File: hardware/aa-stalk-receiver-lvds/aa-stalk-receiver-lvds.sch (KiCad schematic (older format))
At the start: 65 parts, among them CN1 Conn_01x02, CN10 Conn_01x03, CN2 Conn_01x04, CN3 6P6C, CN4 Conn_01x03, CN5 Conn_01x02, CN6 Conn_01x02, CN7 Conn_01x02, CN8 Conn_01x02, CN9 Conn_01x03, Q1 KST10, Q2 MCH3484, Q3 MCH3484, U1 AZ1117-5.0, U2 MIC5504-3.3YM5, U3 LM4562, U4 FIN1028, U5 MC3486N

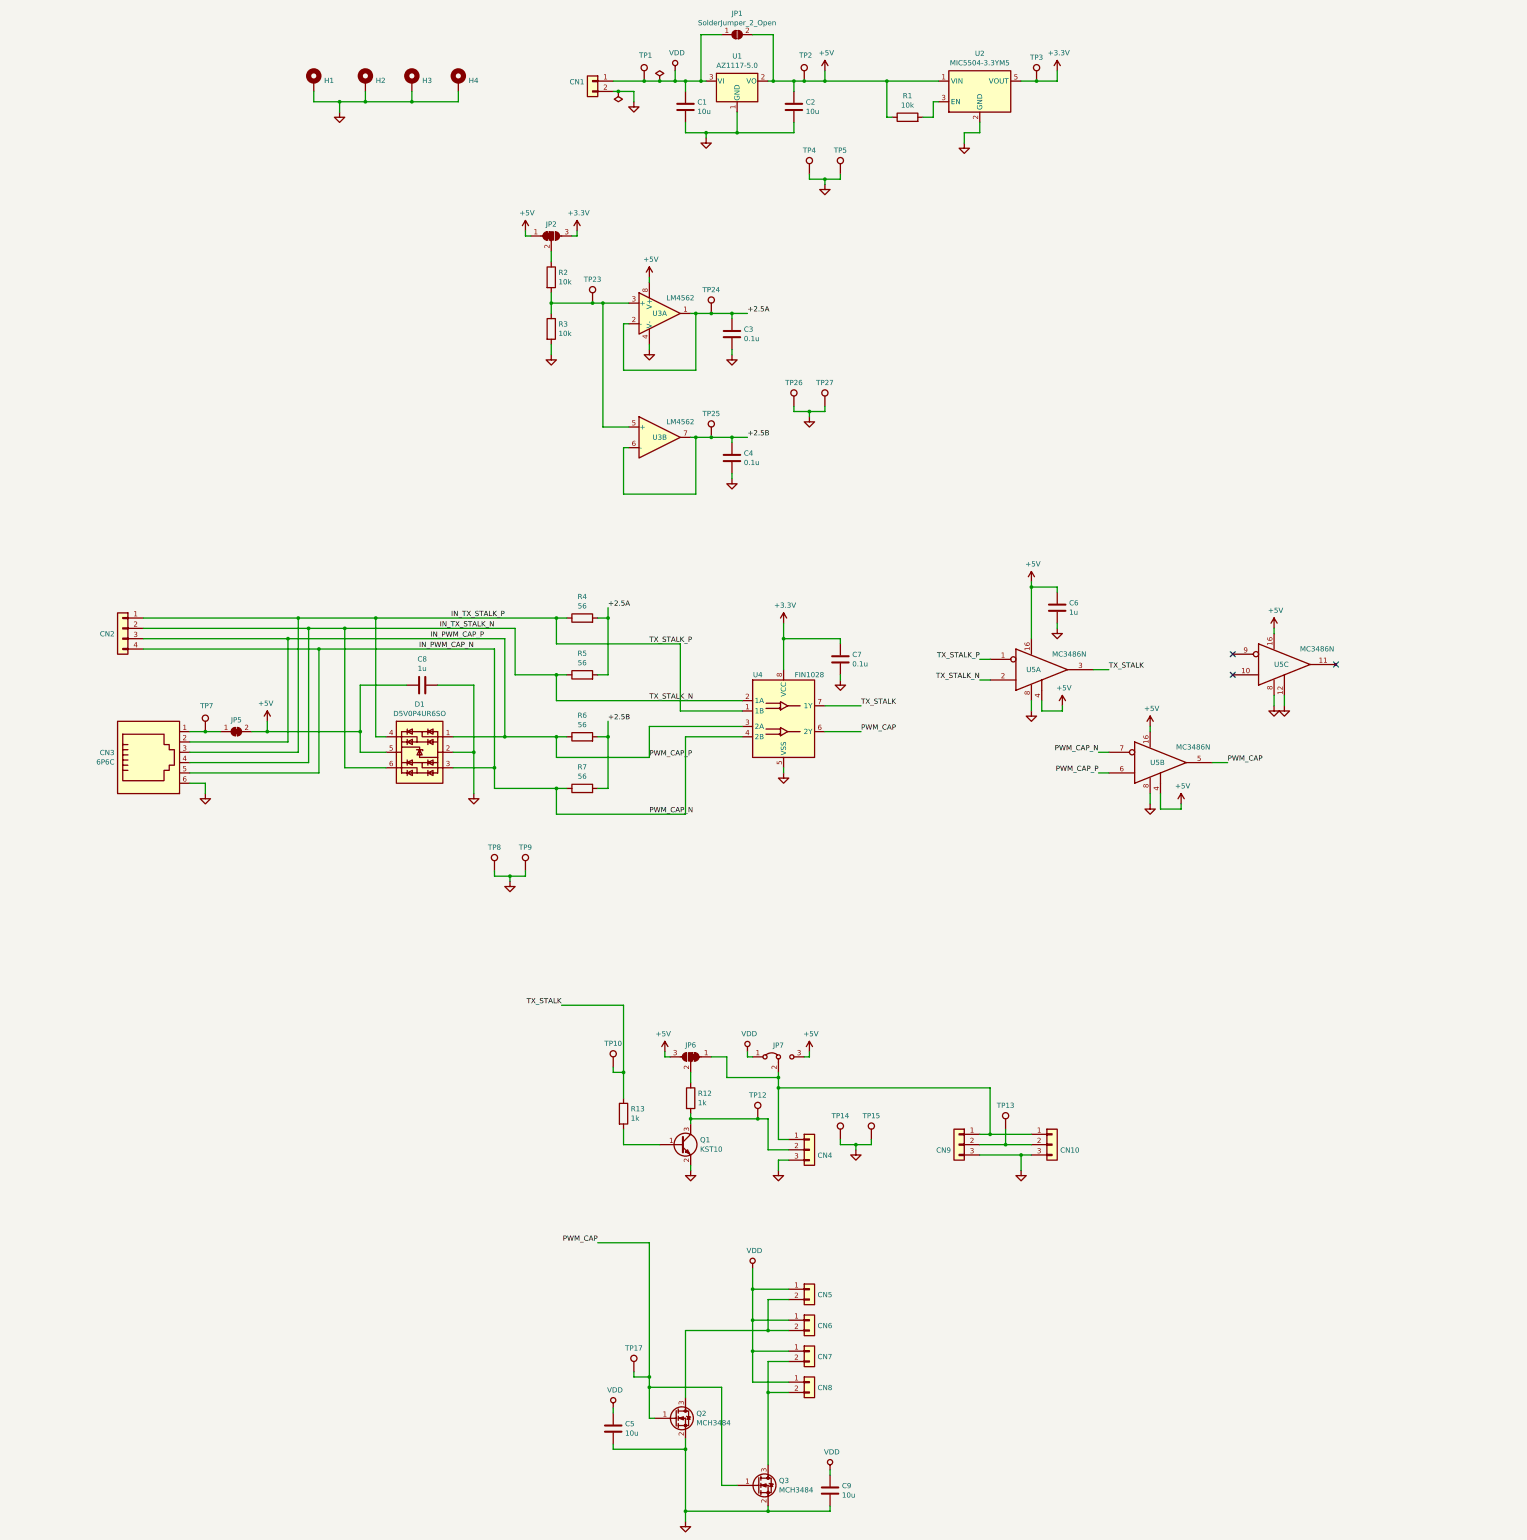
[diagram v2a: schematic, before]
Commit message: Add power distro board, resolve some todos, finish a coherent layout of the panel receiver
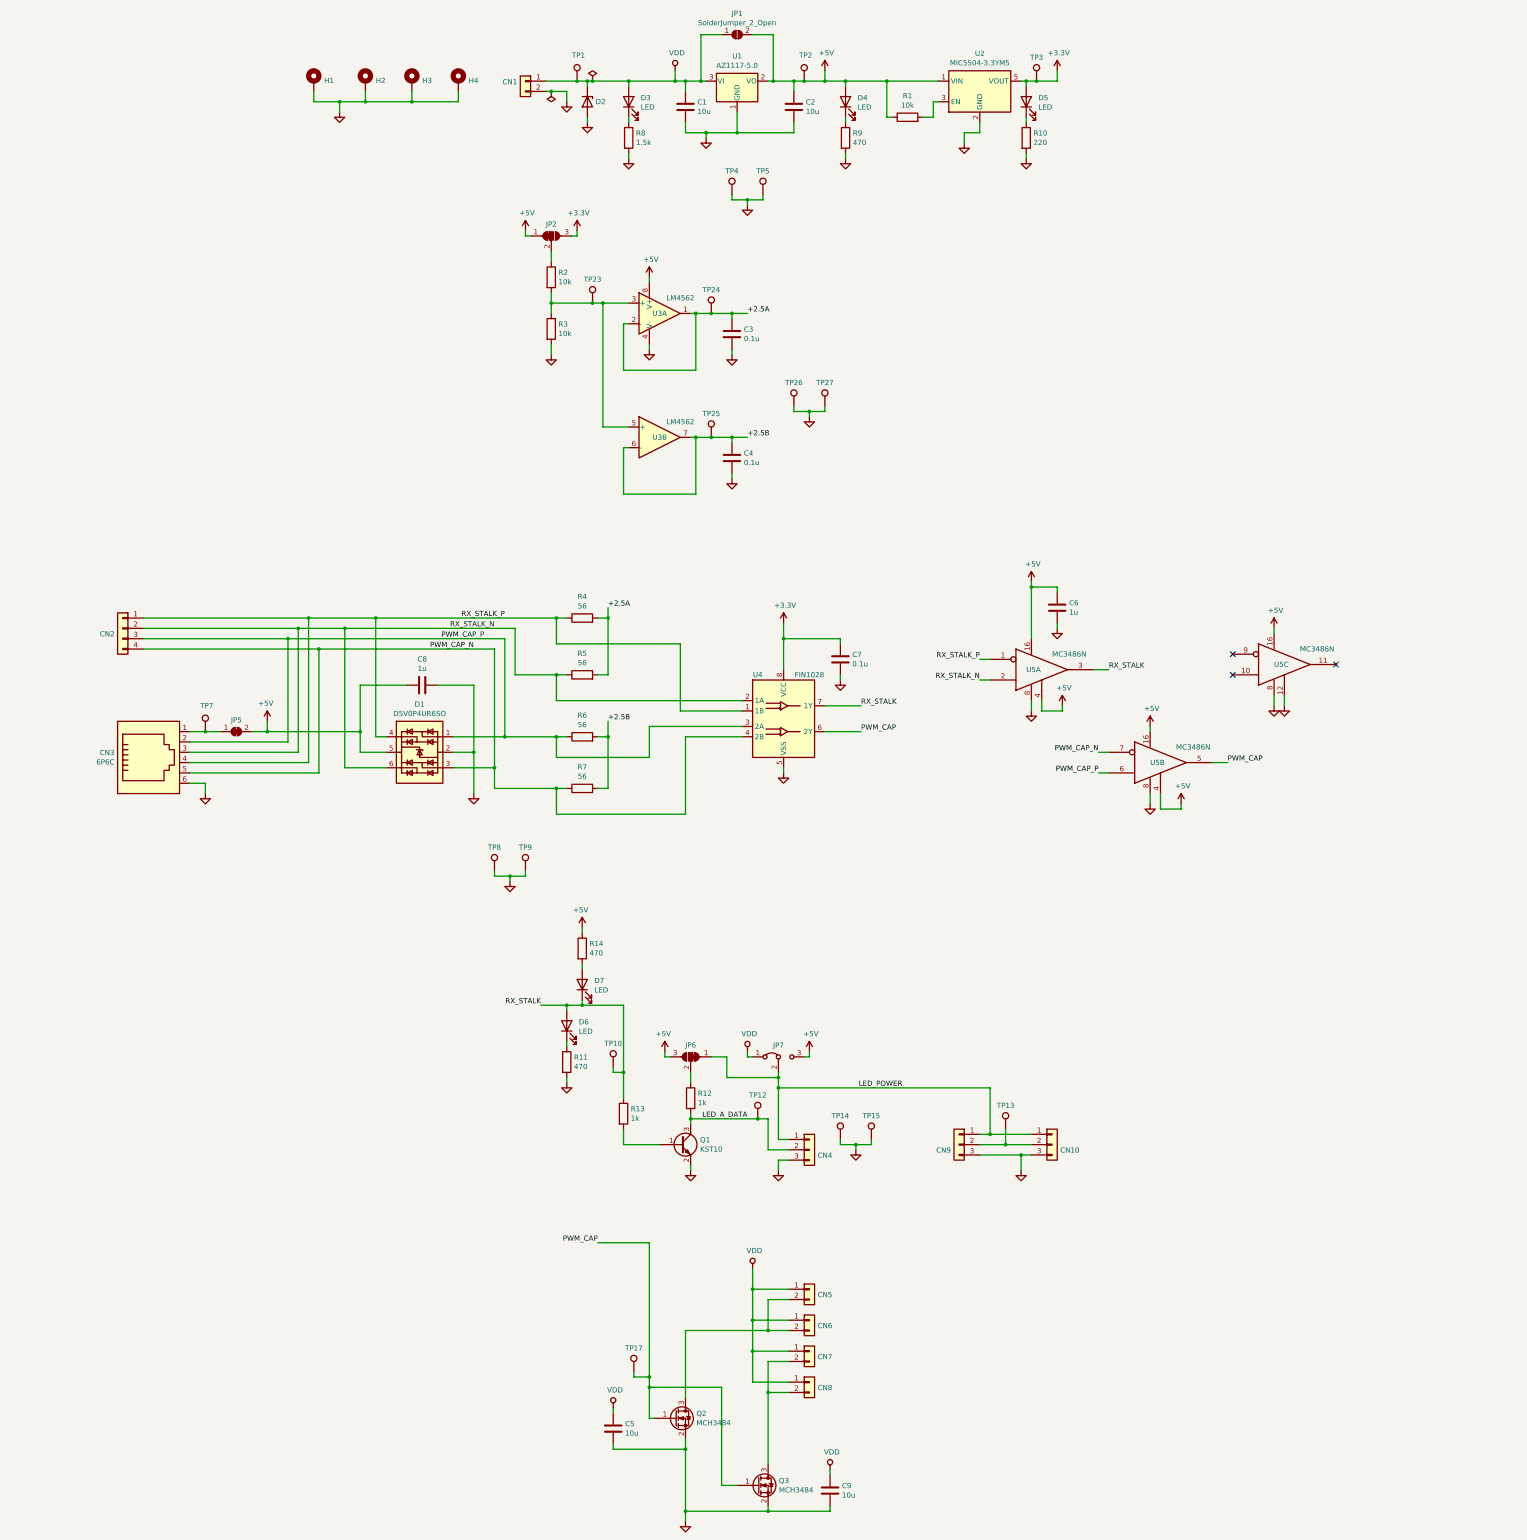
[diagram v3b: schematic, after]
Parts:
- added D2: D_Zener, aa-stalk-receiver-lvds:D_SOD-923, symbol Device:D_Zener
- added D3, D4, D5, D6, D7: LED, Diode_SMD:D_0603_1608Metric, symbol Device:LED
- added R10: 220, Resistor_SMD:R_0603_1608Metric, symbol Device:R
- added R11, R14, R9: 470, Resistor_SMD:R_0603_1608Metric, symbol Device:R
- added R8: 1.5k, Resistor_SMD:R_0603_1608Metric, symbol Device:R
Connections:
- net +3V3: now also D5.2 (A)
- net +5V: now also D4.2 (A), R14.1
- net GND: now also D2.2 (A), R10.2, R11.2, R8.2, R9.2
- net VDD: now also D2.1 (K), D3.2 (A)
- net LED_POWER: now reaches CN10.1 (Pin_1), CN4.1 (Pin_1), CN9.1 (Pin_1), JP6.1 (A), JP7.2 (C)
- net LED_A_DATA: now reaches CN4.2 (Pin_2), Q1.3 (C), R12.2, TP12.1
- net IN_PWM_CAP_N renamed PWM_CAP_N
- net IN_PWM_CAP_P renamed PWM_CAP_P
- net IN_TX_STALK_N renamed RX_STALK_N
- net RX_STALK_N: now also CN3.3; no longer CN3.4
- net IN_TX_STALK_P renamed RX_STALK_P
- net RX_STALK_P: now also CN3.4; no longer CN3.3
- net TX_STALK renamed RX_STALK
- net RX_STALK: now also D6.2 (A), D7.1 (K)
- new net: D4.1 (K), R9.1
- new net: D3.1 (K), R8.1
- new net: D5.1 (K), R10.1
- new net: D6.1 (K), R11.1
- new net: D7.2 (A), R14.2
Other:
- moved on the sheet: CN1, TP1, TP4, TP5

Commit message: Update to use a shared schematic component/footprint library
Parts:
- CN3: footprint aa-stalk-receiver-lvds:6P6C_Assmann_A-2014-1-4 -> aa-shared:6P6C_Assmann_A-2014-1-4
- D1: symbol aa-stalk-receiver-lvds:D5V0P4UR6SO -> aa-shared:D5V0P4UR6SO
- D2: footprint aa-stalk-receiver-lvds:D_SOD-923 -> aa-shared:D_SOD-923
- U4: symbol aa-stalk-receiver-lvds:FIN1028 -> aa-shared:FIN1028
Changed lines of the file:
@@
 	8900 1850 8950 1850
 $Comp
-L aa-stalk-receiver-lvds:D5V0P4UR6SO D1
+L aa-shared:D5V0P4UR6SO D1
 U 1 1 5FA1B995
 P 7700 8250
@@
 F 0 "CN3" H 4720 8254 50  0000 R CNN
 F 1 "6P6C" H 4720 8345 50  0000 R CNN
-F 2 "aa-stalk-receiver-lvds:6P6C_Assmann_A-2014-1-4" V 5050 8275 50  0001 C CNN
+F 2 "aa-shared:6P6C_Assmann_A-2014-1-4" V 5050 8275 50  0001 C CNN
 F 3 "~" V 5050 8275 50  0001 C CNN
 	1    5050 8250
@@
 	9000 8100 9000 8300
 $Comp
-L aa-stalk-receiver-lvds:FIN1028 U4
+L aa-shared:FIN1028 U4
 U 1 1 5D2785D3
 P 11200 7750
@@
 F 0 "D2" V 9300 2029 50  0000 L CNN
 F 1 "D_Zener" V 9345 2029 50  0001 L CNN
-F 2 "aa-stalk-receiver-lvds:D_SOD-923" H 9300 1950 50  0001 C CNN
+F 2 "aa-shared:D_SOD-923" H 9300 1950 50  0001 C CNN
 F 3 "~" H 9300 1950 50  0001 C CNN
 	1    9300 1950

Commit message: Substantial rework of system, new layouts done for daughterboard, power, stalk receiver
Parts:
- removed C1, C2: 10u, Capacitor_SMD:C_0805_2012Metric, symbol Device:C
- removed C7: 0.1u, Capacitor_SMD:C_0805_2012Metric, symbol Device:C
- removed C8: 1u, Capacitor_SMD:C_0805_2012Metric, symbol Device:C
- removed D1: D5V0P4UR6SO, Package_TO_SOT_SMD:SOT-23-6, symbol aa-shared:D5V0P4UR6SO
- removed D5: LED, Diode_SMD:D_0603_1608Metric, symbol Device:LED
- removed JP1: SolderJumper_2_Open, Jumper:SolderJumper-2_P1.3mm_Open_RoundedPad1.0x1.5mm, symbol Jumper:SolderJumper_2_Open
- removed JP2: SolderJumper_3_Bridged12, Jumper:SolderJumper-3_P1.3mm_Bridged12_RoundedPad1.0x1.5mm, symbol Jumper:SolderJumper_3_Bridged12
- removed JP5: SolderJumper_2_Bridged, Jumper:SolderJumper-2_P1.3mm_Bridged_RoundedPad1.0x1.5mm, symbol Jumper:SolderJumper_2_Bridged
- removed JP7: Jumper_3_Bridged12, Connector_PinHeader_2.54mm:PinHeader_1x03_P2.54mm_Vertical, symbol Jumper:Jumper_3_Bridged12
- removed R1, R2, R3: 10k, Resistor_SMD:R_0603_1608Metric, symbol Device:R
- removed R10: 220, Resistor_SMD:R_0603_1608Metric, symbol Device:R
- removed TP14, TP15, TP17, TP23, TP24, TP25, TP26, TP27, TP3, TP7, TP8, TP9: TestPoint, TestPoint:TestPoint_THTPad_D2.0mm_Drill1.0mm, symbol Connector:TestPoint
- removed U1: AZ1117-5.0, Package_TO_SOT_SMD:SOT-223-3_TabPin2, symbol Regulator_Linear:AZ1117-5.0
- removed U2: MIC5504-3.3YM5, Package_TO_SOT_SMD:SOT-23-5, symbol Regulator_Linear:MIC5504-3.3YM5
- removed U3: LM4562, Package_SO:SOIC-8_3.9x4.9mm_P1.27mm, symbol Amplifier_Operational:LM4562
- removed U4: FIN1028, Package_SO:SOIC-8_3.9x4.9mm_P1.27mm, symbol aa-shared:FIN1028
- added C101: 100u, Capacitor_THT:CP_Radial_D10.0mm_P2.50mm_P5.00mm, symbol Device:CP
- added C102: 10u, Capacitor_THT:CP_Radial_D5.0mm_P2.50mm, symbol Device:CP
- added C103: 1u, Capacitor_SMD:C_0805_2012Metric, symbol Device:C
- added C301: 0.1u, Capacitor_SMD:C_0805_2012Metric, symbol Device:C
- added D102: D5V0P4UR6SO, Package_TO_SOT_SMD:SOT-23-6, symbol aa-shared:D5V0P4UR6SO
- added D201, D202, D203, D204: BZX79C2V7, Diode_THT:D_DO-35_SOD27_P7.62mm_Horizontal, symbol Device:D_Zener
- added JP101: Jumper_2_Bridged, Connector_PinHeader_2.54mm:PinHeader_1x02_P2.54mm_Vertical, symbol Jumper:Jumper_2_Bridged
- added TP102: +5V, aa-shared:TestPoint_Loop_D1.80mm_Drill1.0mm_Beaded, symbol Connector:TestPoint
- added TP201: RX_T, aa-shared:TestPoint_Loop_D1.80mm_Drill1.0mm_Beaded, symbol Connector:TestPoint
- added TP202: PWM_T, aa-shared:TestPoint_Loop_D1.80mm_Drill1.0mm_Beaded, symbol Connector:TestPoint
- added TP251, TP252, TP351, TP352, TP361: GND, aa-shared:TestPoint_Loop_D1.80mm_Drill1.0mm_Beaded, symbol Connector:TestPoint
- added TP311: PWM, aa-shared:TestPoint_Loop_D1.80mm_Drill1.0mm_Beaded, symbol Connector:TestPoint
- D101: renamed from D2; value D_Zener -> DF2S16FS
- H1, H2, H3, H4: footprint MountingHole:MountingHole_4.3mm_M4_Pad_Via -> MountingHole:MountingHole_2.7mm_M2.5_Pad_Via
- JP351: renamed from JP6; footprint Jumper:SolderJumper-3_P1.3mm_Bridged12_RoundedPad1.0x1.5mm -> Jumper:SolderJumper-3_P1.3mm_Open_RoundedPad1.0x1.5mm
- TP101: renamed from TP1; value TestPoint -> +12V; footprint TestPoint:TestPoint_THTPad_D2.0mm_Drill1.0mm -> aa-shared:TestPoint_Loop_D1.80mm_Drill1.0mm_Beaded
- TP151: renamed from TP2; value TestPoint -> GND; footprint TestPoint:TestPoint_THTPad_D2.0mm_Drill1.0mm -> aa-shared:TestPoint_Loop_D1.80mm_Drill1.0mm_Beaded
- TP152: renamed from TP4; value TestPoint -> GND; footprint TestPoint:TestPoint_THTPad_D2.0mm_Drill1.0mm -> aa-shared:TestPoint_Loop_D1.80mm_Drill1.0mm_Beaded
- TP153: renamed from TP5; value TestPoint -> GND; footprint TestPoint:TestPoint_THTPad_D2.0mm_Drill1.0mm -> aa-shared:TestPoint_Loop_D1.80mm_Drill1.0mm_Beaded
- TP301: renamed from TP10; value TestPoint -> NRX; footprint TestPoint:TestPoint_THTPad_D2.0mm_Drill1.0mm -> aa-shared:TestPoint_Loop_D1.80mm_Drill1.0mm_Beaded
- TP302: renamed from TP12; value TestPoint -> A_D; footprint TestPoint:TestPoint_THTPad_D2.0mm_Drill1.0mm -> aa-shared:TestPoint_Loop_D1.80mm_Drill1.0mm_Beaded
- TP303: renamed from TP13; value TestPoint -> C_D; footprint TestPoint:TestPoint_THTPad_D2.0mm_Drill1.0mm -> aa-shared:TestPoint_Loop_D1.80mm_Drill1.0mm_Beaded
- U201: renamed from U5; value MC3486N -> ST26C32
- renumbered C3 to C202, C4 to C203, C6 to C204, C5 to C311, C9 to C312, CN1 to CN101, CN3 to CN102, CN2 to CN151, CN4 to CN301, CN9 to CN302, CN10 to CN303, CN5 to CN311, CN6 to CN312, CN7 to CN313, CN8 to CN314, D3 to D151, D4 to D152, D7 to D351, D6 to D352, Q1 to Q301, Q2 to Q311, Q3 to Q312, R8 to R151, R9 to R152, R4 to R201, R5 to R202, R6 to R203, R7 to R204, R13 to R301, R12 to R302, R14 to R351, R11 to R352
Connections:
- net labels added: +12V, LED_C_DATA, N_RX_STALK, VIN
- net labels removed: +2.5A, +2.5B, +3.3V, LED_POWER, RX_STALK, VDD
- wire segments 309 -> 241
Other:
- note added: "2.7V Zeners\nprovide loose\nregulation to\nreduce large\nsignal (>500mV)\nlow freq CM\nnoise and DC\nbias\nThey may be\nreplaced with\n1k-2k resistors"
- moved on the sheet: C202, C203, C204, C311, C312, CN101, CN102, CN151, CN301, CN302, CN303, CN311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
